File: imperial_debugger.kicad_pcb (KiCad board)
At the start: 4 copper layers, 88.6 x 50.8 mm, 137 parts, among them J1 USB_B_Micro, J2 Conn_01x04_Male, J3 Conn_01x04_Male, J4 Conn_01x04_Male, J5 Conn_01x06_Male, J6 Conn_01x05_Male, J7 Conn_01x05_Male, J8 Conn_01x05_Male, J9 Conn_01x04_Male, U1 LM2594M-3.3, U10 74LVC1G3157, U11 SP330EEY-L, U12 TXS0104EDR, U13 74LVC1G3157, U14 MAX3222EIPW, U2 93LC54B, U3 FT4232H, U4 74LVC1G3157, U5 SP330EEY-L, U6 74LVC1G3157, U7 TLV75525PDBV, U8 TXS0104EDR, U9 TLV75518PDBV, Y1 12MHz

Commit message: Updates as we do routing.
Changed discrete jumpres to a 2x4 block and 2x3 block, 2mm pitch.

Started routing each tranciever block
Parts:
- removed JP10, JP11, JP13, JP14, JP16, JP17, JP18, JP2, JP20, JP21, JP22, JP24, JP25, JP26, JP3, JP5, JP6, JP7, JP9: Jumper, Connector_PinHeader_2.00mm:PinHeader_1x02_P2.00mm_Vertical_SMD_Pin1Left
- added JP27: Jumper, Connector_PinHeader_2.00mm:PinHeader_1x02_P2.00mm_Vertical_SMD_Pin1Left, F.Cu at (135.6, 82.7)
- added JP28: Jumper, Connector_PinHeader_2.00mm:PinHeader_1x02_P2.00mm_Vertical_SMD_Pin1Left, F.Cu at (190.6, 132.1)
- added JP29: Jumper, Connector_PinHeader_2.00mm:PinHeader_1x02_P2.00mm_Vertical_SMD_Pin1Left, F.Cu at (135.8, 88.3)
- added JP30: Jumper, Connector_PinHeader_2.00mm:PinHeader_1x02_P2.00mm_Vertical_SMD_Pin1Left, F.Cu at (190.6, 137.7)
- added R31: 120R, Resistor_SMD:R_0603_1608Metric_Pad0.98x0.95mm_HandSolder, F.Cu at (140.3, 86.7)
- added R32: 120R, Resistor_SMD:R_0603_1608Metric_Pad0.98x0.95mm_HandSolder, F.Cu at (195.3, 136.1)
- added R33: 120R, Resistor_SMD:R_0603_1608Metric_Pad0.98x0.95mm_HandSolder, F.Cu at (140.3, 89.3)
- added R34: 120R, Resistor_SMD:R_0603_1608Metric_Pad0.98x0.95mm_HandSolder, F.Cu at (195.3, 138.7)
- JP1, JP12: footprint Connector_PinHeader_2.00mm:PinHeader_1x02_P2.00mm_Vertical_SMD_Pin1Left -> Connector_PinHeader_2.00mm:PinHeader_2x03_P2.00mm_Vertical_SMD
- JP15: footprint Connector_PinHeader_2.00mm:PinHeader_1x02_P2.00mm_Vertical_SMD_Pin1Left -> Connector_PinHeader_1.27mm:PinHeader_2x04_P1.27mm_Vertical_SMD
- JP19, JP23, JP4, JP8: footprint Connector_PinHeader_2.00mm:PinHeader_1x02_P2.00mm_Vertical_SMD_Pin1Left -> Connector_PinHeader_2.00mm:PinHeader_2x04_P2.00mm_Vertical_SMD
- moved J8 306.7 mm to (199.3, 131.1)
- moved U11 244.0 mm to (143.9, 133.2)
- moved J7 242.0 mm to (143.9, 81.7)
- moved J5 240.6 mm to (143.6, 58.5)
- moved JP12 239.7 mm to (153.7, 143.0), turned to 90 degrees
- moved J6 234.8 mm to (142.6, 30.9)
- moved R13 228.4 mm to (153.7, 137.4), turned to 270 degrees
- moved J4 218.9 mm to (116.3, 132.2)
- moved JP19 216.3 mm to (129.3, 132.1)
- moved R14 213.1 mm to (155.6, 137.4), turned to 270 degrees
- moved R19 211.9 mm to (134.1, 146.3)
- moved U8 211.8 mm to (120.5, 66.0), turned to 180 degrees
- moved R12 209.3 mm to (151.6, 137.4), turned to 270 degrees
- moved C30 208.1 mm to (151.9, 121.2)
- moved J9 206.4 mm to (118.5, 38.2)
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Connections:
- C31 pad 1: /Transceivers/VREF -> Vdrive
- J5 pad 6: /Transceivers/VREF -> Vdrive
- JP15 pad 2: /Transceivers/VREF -> Vdrive
- JP4 pad 1: ADBUS0 -> ADBUS3
- JP4 pad 2: /Transceivers/TXD_1 -> /Transceivers/CTSn_1
- R11 pad 2: Net-(JP3-Pad2) -> Net-(JP1-Pad6)
- R14 pad 2: Net-(JP14-Pad2) -> Net-(JP12-Pad6)
- U11 pad 12: Net-(JP14-Pad2) -> Net-(JP12-Pad6)
- U12 pad 14: /Transceivers/VREF -> Vdrive
- U5 pad 12: Net-(JP3-Pad2) -> Net-(JP1-Pad6)
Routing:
- net GND: track 24.1 -> 73.3 mm, vias 10 -> 40
- net /Transceivers/PORT_3_RTS: track 0.00 -> 31.8 mm, vias 0 -> 1
- net /Transceivers/PORT_3_TXD: track 0.00 -> 29.8 mm, vias 0 -> 2
- net +3V3: track 24.3 -> 53.1 mm, vias 3 -> 16
- net Net-(R15-Pad2): track 0.00 -> 27.9 mm, vias 0 -> 2
- net VBUS: track 6.36 -> 33.7 mm
- net Vdrive: track 0.00 -> 26.5 mm, vias 0 -> 4
- net /Transceivers/PORT_3_CTS: track 0.00 -> 25.1 mm, vias 0 -> 1
- net /Transceivers/FULLn_3: track 0.00 -> 24.6 mm, vias 0 -> 4
- net /Transceivers/PORT_3_RXD: track 0.00 -> 23.2 mm, vias 0 -> 1
- net Net-(JP1-Pad6): track 0.00 -> 20.0 mm, vias 0 -> 2
- net /Transceivers/PORT_2_CTS: track 0.00 -> 17.7 mm, vias 0 -> 1
- net /Transceivers/PORT_2_RTS: track 0.00 -> 17.2 mm, vias 0 -> 1
- net ADBUS1: track 0.00 -> 15.7 mm, vias 0 -> 1
- net /Transceivers/RXD_2: track 0.00 -> 15.2 mm
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- added copper zone on In1.Cu, net +1V8
- added copper zone on In1.Cu, net +3V3
- added copper zone on B.Cu, net GND
- added copper zone on In1.Cu, net Vdrive
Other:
- board size 88.6 x 50.8 mm -> 7.5 x 2 mm

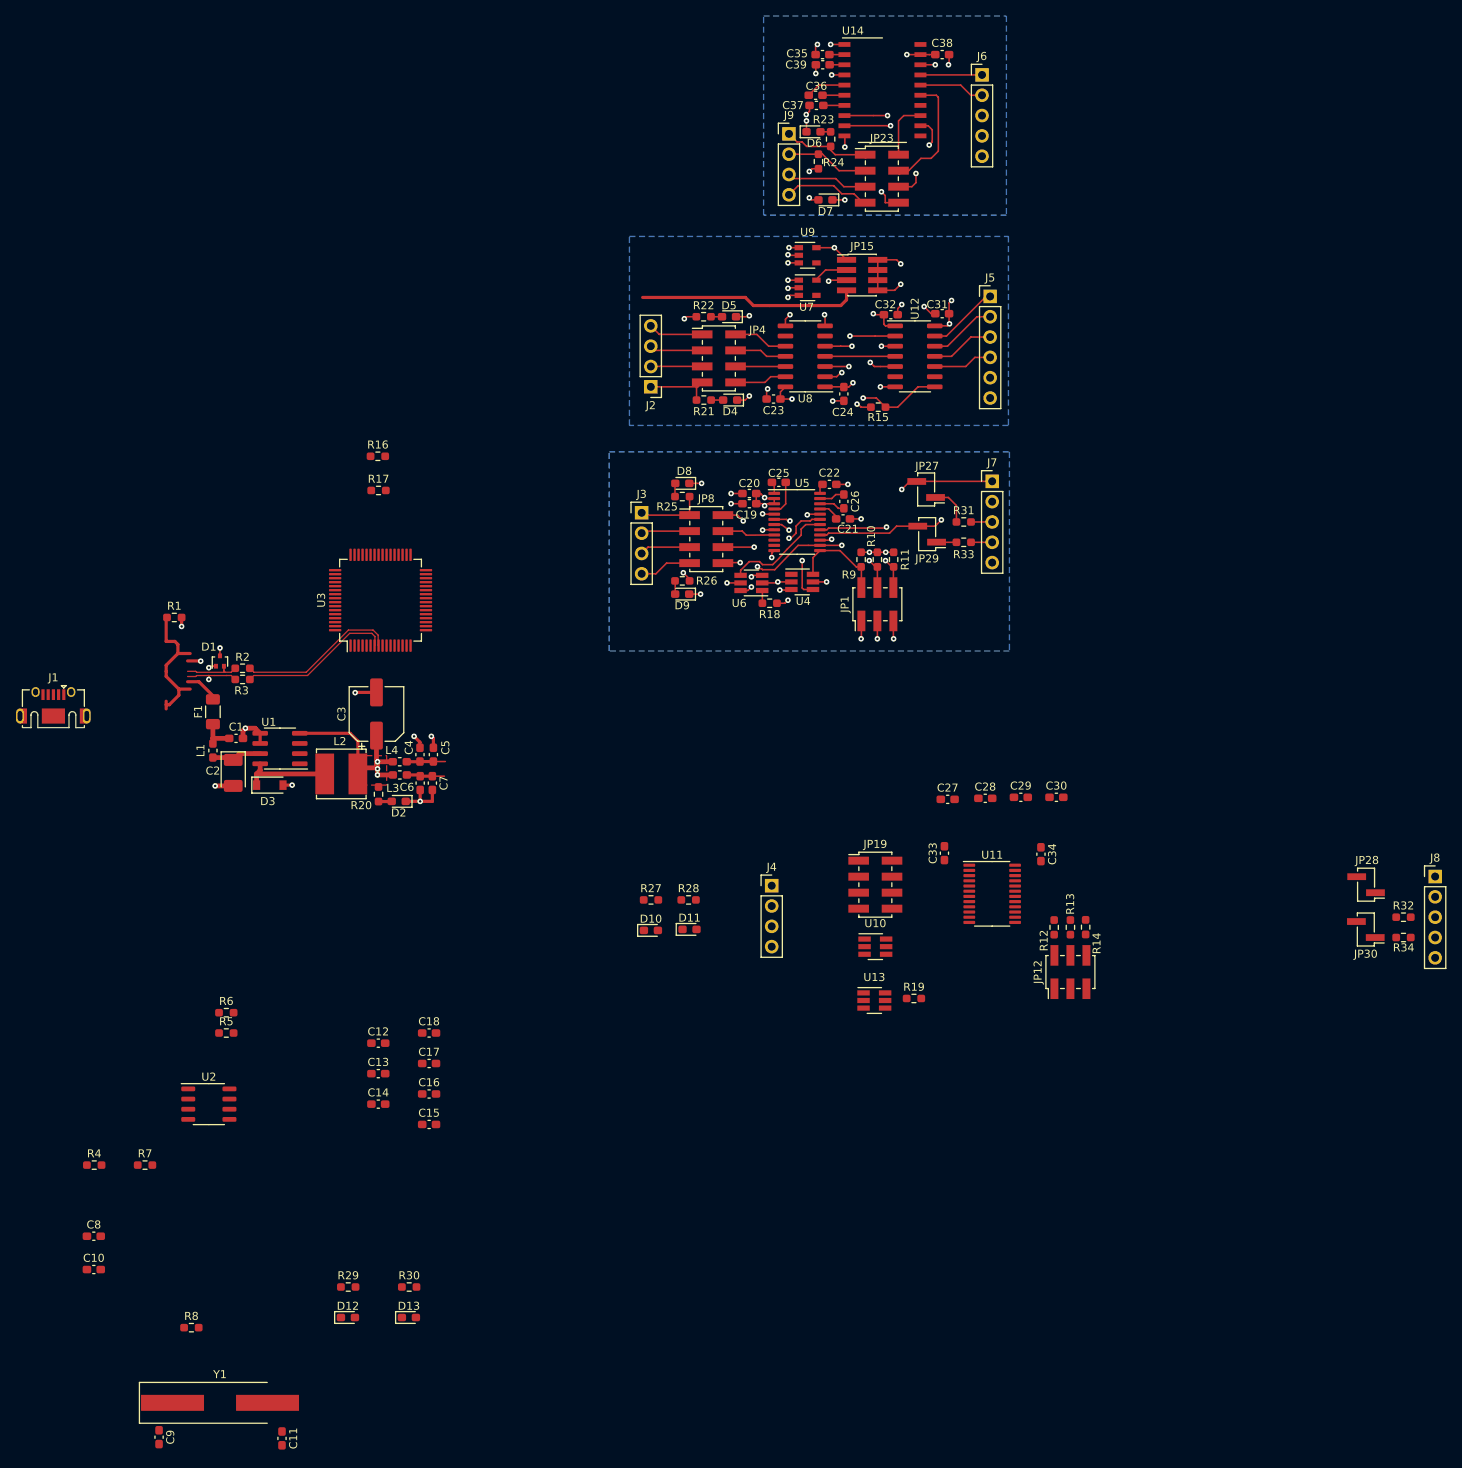
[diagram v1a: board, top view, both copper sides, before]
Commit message: Almost fully routed.. lots of DRC's to sort out.
Also need to get correct pcb parameters to do more checks.
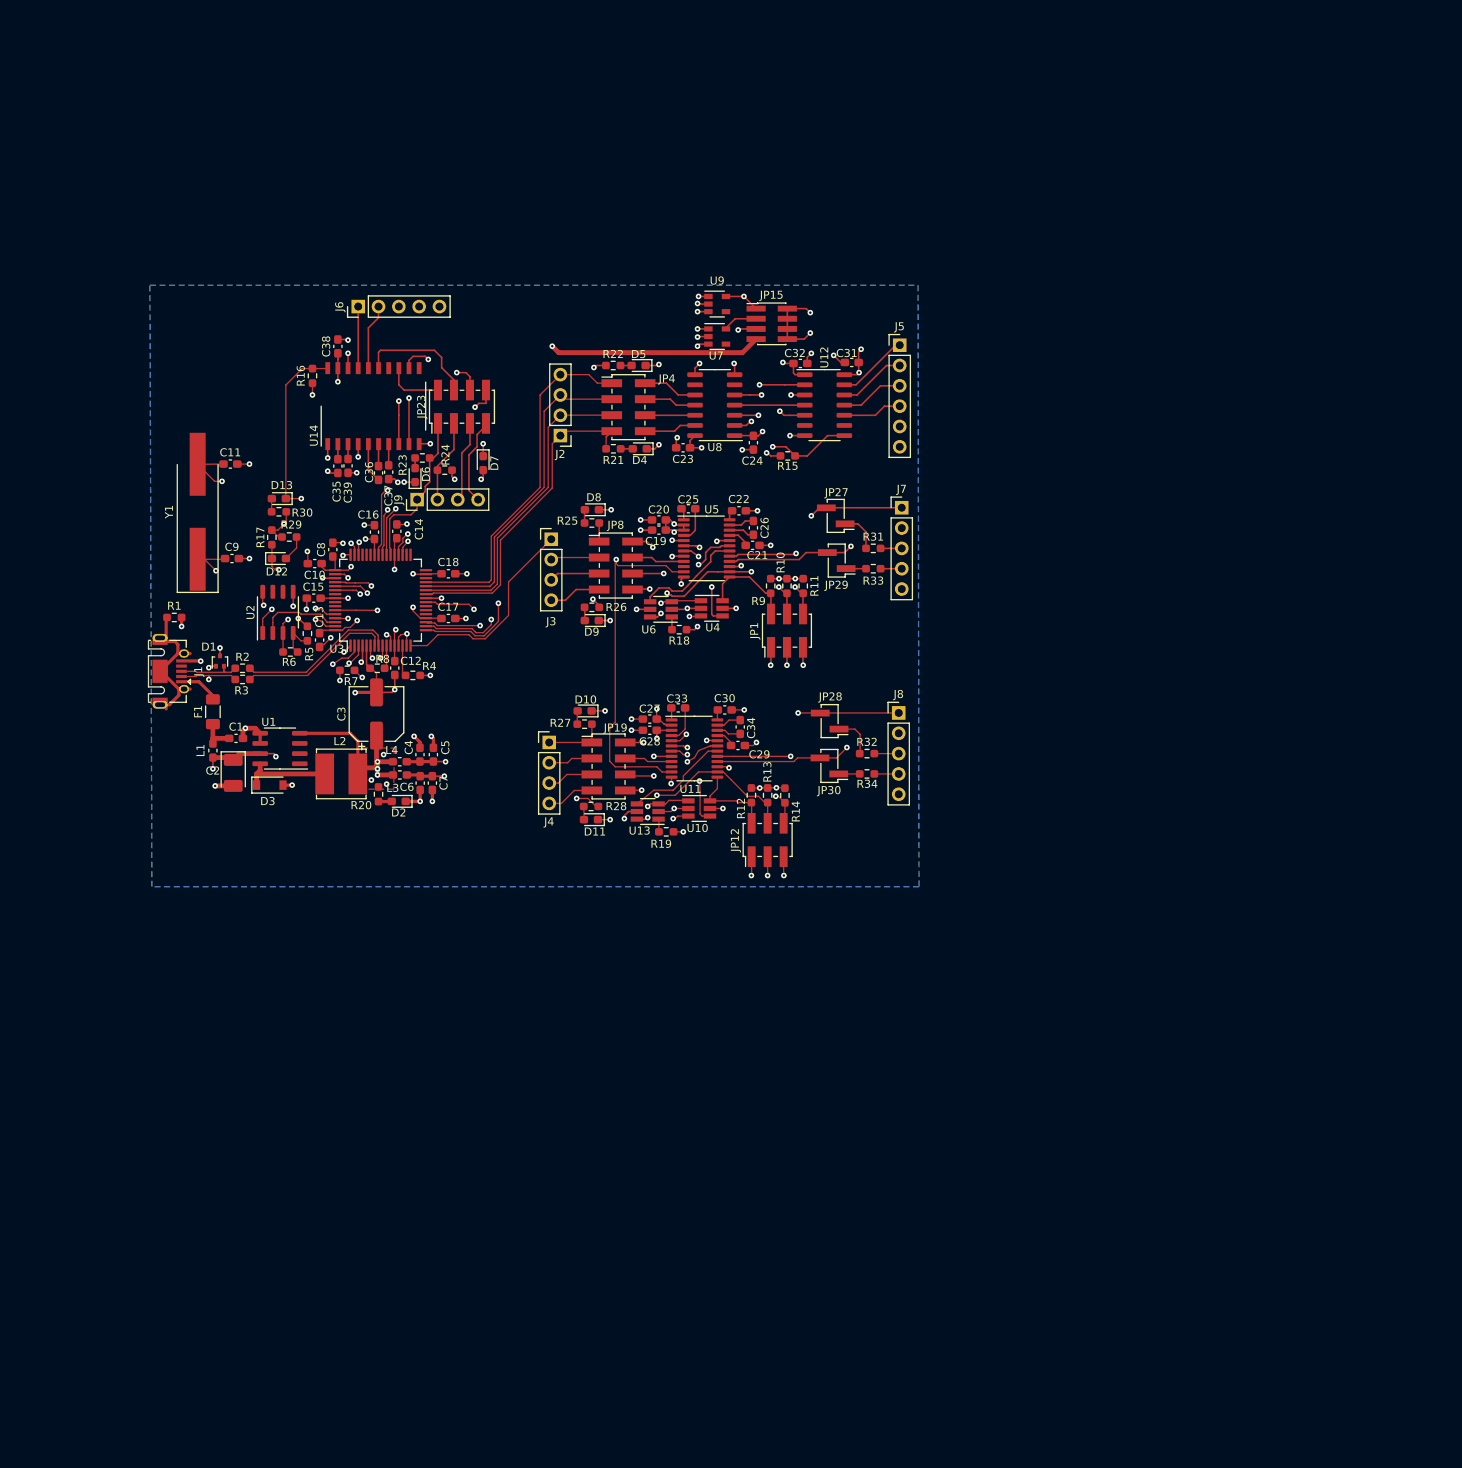
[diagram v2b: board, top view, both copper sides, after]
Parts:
- moved C11 122.0 mm to (48.7, 79.5), turned to 0 degrees
- moved Y1 111.4 mm to (44.6, 85.5), turned to 90 degrees
- moved C9 110.2 mm to (48.9, 91.3), turned to 0 degrees
- moved D13 103.6 mm to (54.7, 83.8), turned to 180 degrees
- moved R30 98.3 mm to (54.7, 85.5)
- moved D12 95.3 mm to (54.7, 91.3)
- moved R29 94.0 mm to (56.0, 88.6), turned to 180 degrees
- moved C10 92.5 mm to (59.2, 91.9), turned to 180 degrees
- moved C8 90.9 mm to (61.5, 90.2), turned to 90 degrees
- moved R8 85.6 mm to (67.0, 105.0)
- moved C38 83.9 mm to (62.1, 64.8), turned to 90 degrees
- moved J6 83.2 mm to (64.6, 59.8), turned to 90 degrees
- moved C35 79.5 mm to (62.1, 79.8), turned to 90 degrees
- moved C39 77.7 mm to (63.4, 79.7), turned to 270 degrees
- moved U14 74.9 mm to (66.5, 72.3), turned to 90 degrees
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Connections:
- C10 pad 1: +3V3 -> /USB and Power/VREGOUT
- C12 pad 1: +3V3 -> /USB and Power/VREGOUT
- C13 pad 1: +3V3 -> /USB and Power/VREGOUT
- C14 pad 1: +3V3 -> /USB and Power/VREGOUT
- C8 pad 1: +3V3 -> /USB and Power/VREGOUT
- J2 pad 1: ADBUS0 -> BDBUS0
- J2 pad 2: ADBUS1 -> BDBUS1
- J2 pad 3: ADBUS2 -> BDBUS2
- J2 pad 4: ADBUS3 -> BDBUS3
- J3 pad 1: CDBUS0 -> ADBUS0
- J3 pad 2: CDBUS1 -> ADBUS1
- J3 pad 3: CDBUS2 -> ADBUS2
- J3 pad 4: CDBUS3 -> ADBUS3
- J9 pad 1: BDBUS0 -> CDBUS0
- J9 pad 2: BDBUS1 -> CDBUS1
- J9 pad 3: BDBUS2 -> CDBUS2
- J9 pad 4: BDBUS3 -> CDBUS3
- JP23 pad 1: BDBUS0 -> CDBUS0
- JP23 pad 3: BDBUS1 -> CDBUS1
- JP23 pad 5: BDBUS2 -> CDBUS2
- JP23 pad 7: BDBUS3 -> CDBUS3
- JP4 pad 1: ADBUS3 -> BDBUS3
- JP4 pad 3: ADBUS2 -> BDBUS2
- JP4 pad 5: ADBUS1 -> BDBUS1
- JP4 pad 7: ADBUS0 -> BDBUS0
- JP8 pad 1: CDBUS0 -> ADBUS0
- JP8 pad 3: CDBUS1 -> ADBUS1
- JP8 pad 5: CDBUS2 -> ADBUS2
- JP8 pad 7: CDBUS3 -> ADBUS3
- R21 pad 2: ADBUS0 -> BDBUS0
- R22 pad 2: ADBUS1 -> BDBUS1
- R23 pad 2: BDBUS0 -> CDBUS0
- R24 pad 2: BDBUS1 -> CDBUS1
- R25 pad 2: CDBUS0 -> ADBUS0
- R26 pad 2: CDBUS1 -> ADBUS1
- U3 pad 12: +3V3 -> /USB and Power/VREGOUT
- U3 pad 33: BDBUS0 -> BDBUS6
- U3 pad 37: +3V3 -> /USB and Power/VREGOUT
- U3 pad 49: +3V3 -> /USB and Power/VREGOUT
- U3 pad 64: +3V3 -> /USB and Power/VREGOUT
- U4 pad 1: CDBUS7 -> ADBUS7
- U6 pad 3: CDBUS7 -> ADBUS7
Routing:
- net SUSPEND#: track 0.00 -> 112.0 mm, vias 0 -> 3
- net VBUS: track 33.7 -> 131.0 mm, vias 0 -> 3
- net GND: track 73.3 -> 138.6 mm, vias 40 -> 74
- net DDBUS7: track 0.00 -> 59.6 mm, vias 0 -> 2
- net DDBUS1: track 0.00 -> 51.0 mm, vias 0 -> 2
- net DDBUS3: track 0.00 -> 46.7 mm, vias 0 -> 1
- net DDBUS0: track 0.00 -> 45.5 mm, vias 0 -> 1
- net DDBUS2: track 0.00 -> 44.4 mm, vias 0 -> 1
- net +3V3: track 53.1 -> 95.1 mm, vias 16 -> 35
- net Net-(C11-Pad1): track 0.00 -> 41.6 mm, vias 0 -> 2
- net ADBUS7: track 0.00 -> 39.6 mm, vias 0 -> 2
- net BDBUS1: track 10.4 -> 49.3 mm, vias 0 -> 1
- net /Transceivers/PORT_4_RTS: track 0.00 -> 32.5 mm, vias 0 -> 1
- net BDBUS3: track 12.0 -> 44.4 mm
- net BDBUS2: track 10.8 -> 42.2 mm
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- added copper zone on In1.Cu, net /USB and Power/VREGOUT
- added copper zone on In1.Cu, net VBUS
- added copper zone on In1.Cu, net VPHY
- added copper zone on In1.Cu, net VPLL
- removed copper zone on In1.Cu, net GND
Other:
- board size 7.5 x 2 mm -> 2 x 7.5 mm
